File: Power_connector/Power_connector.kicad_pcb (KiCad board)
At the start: 2 copper layers, 33 parts, among them J1 XT60_F, J10 XT60_F, J11 XT60_F, J12 XT60_F, J2 XT60_Male, J3 XT60_F, J4 XT60_F, J5 Screw_Terminal_01x02, J6 XT60_F, J7 XT60_F, J8 XT60_F, J9 XT60_F, Q1 IRFS7530, Q2 IRFS7530, Q3 IRFS7530

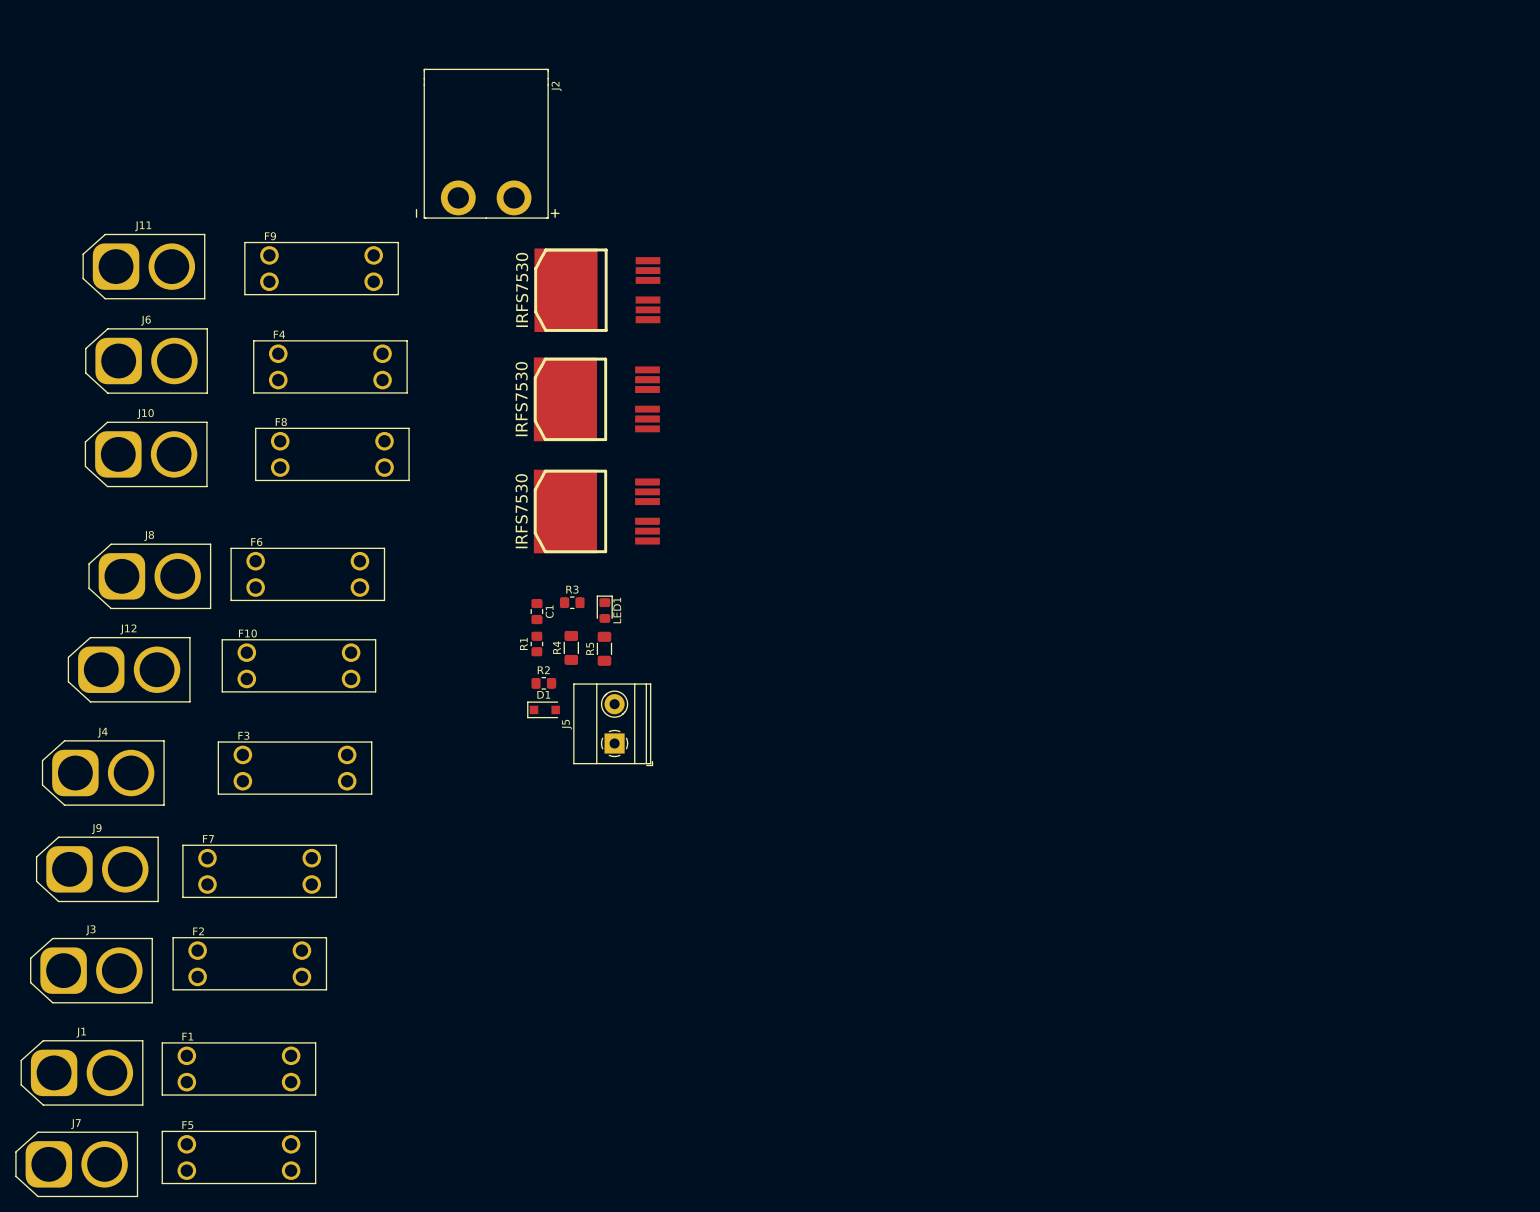
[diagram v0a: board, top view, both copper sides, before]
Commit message: added power board
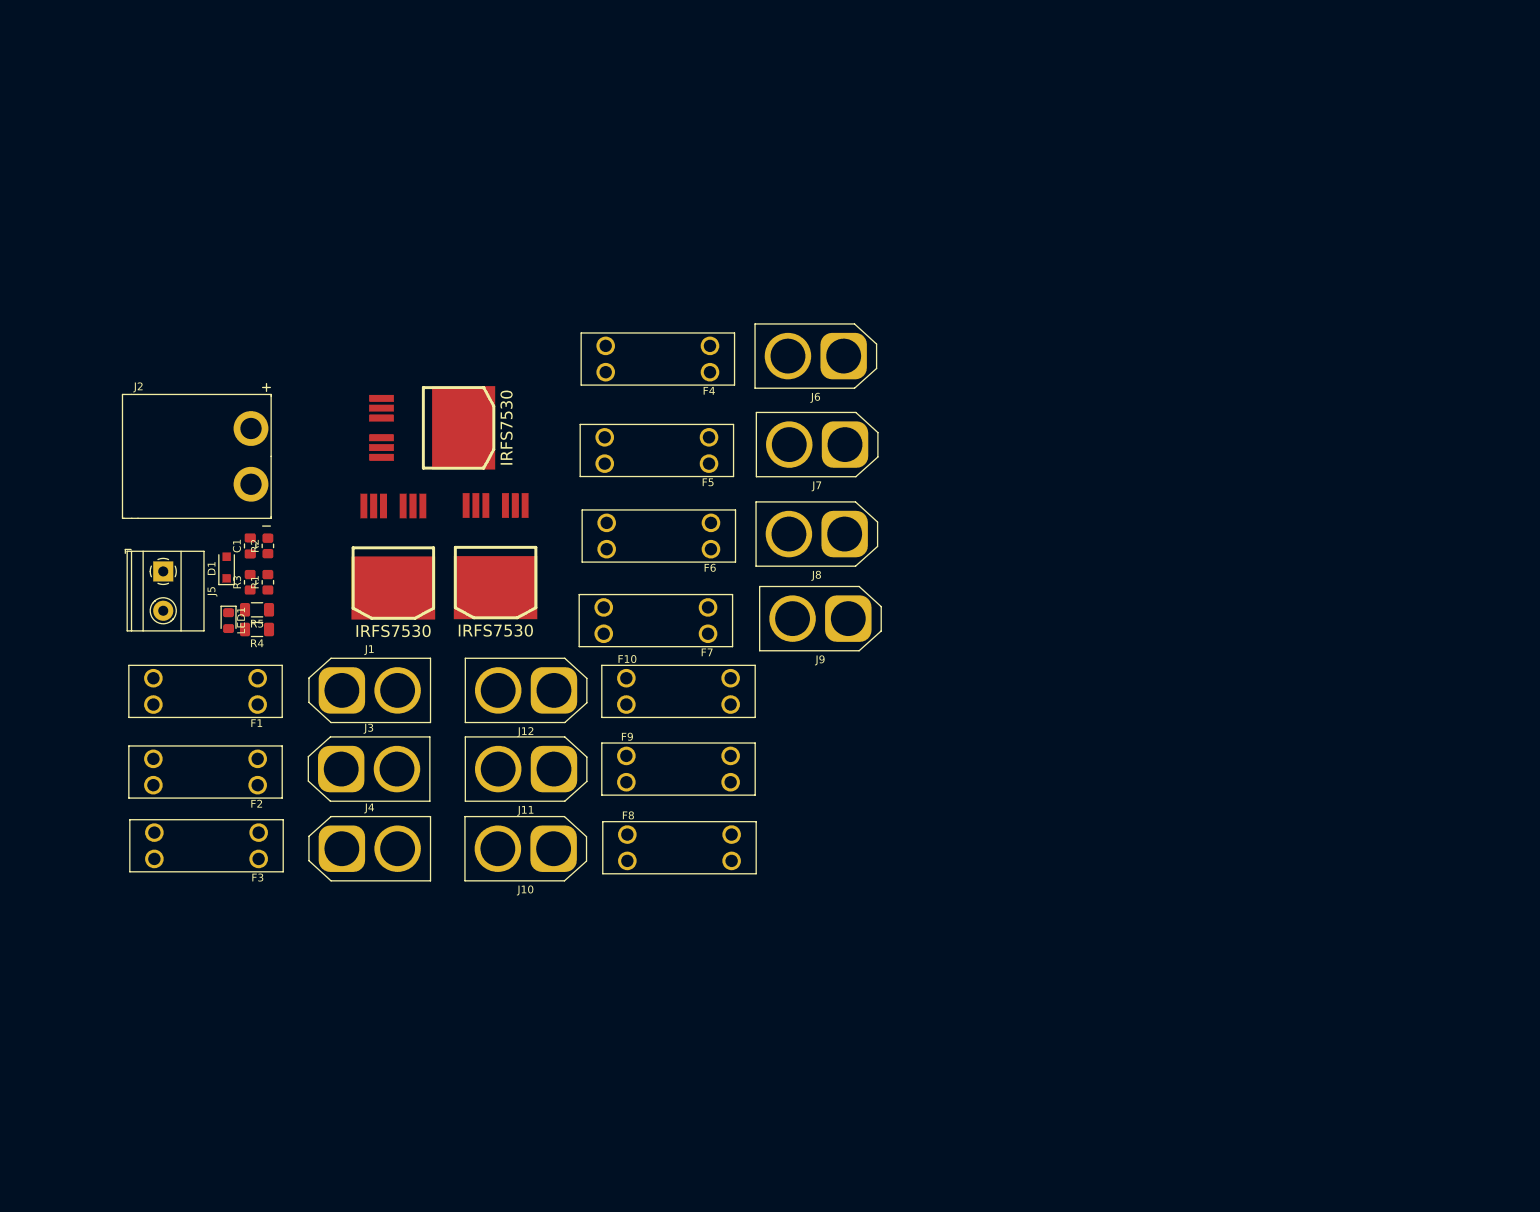
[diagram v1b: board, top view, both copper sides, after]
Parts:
- moved J7 138.6 mm to (162.5, 96.0), turned to 180 degrees
- moved F5 106.1 mm to (138.2, 96.8), turned to 180 degrees
- moved J9 105.7 mm to (162.9, 118.5), turned to 180 degrees
- moved J6 93.6 mm to (162.3, 84.6), turned to 180 degrees
- moved J8 93.5 mm to (162.4, 107.6), turned to 180 degrees
- moved J11 86.1 mm to (124.9, 137.9), turned to 180 degrees
- moved F9 79.4 mm to (141.0, 137.9)
- moved J10 75.9 mm to (124.8, 148.2), turned to 180 degrees
- moved F8 67.8 mm to (141.1, 148.1)
- moved J5 62.4 mm to (74.4, 112.4), turned to -90 degrees
- moved J1 61.8 mm to (97.5, 127.8)
- moved F7 60.6 mm to (138.0, 118.7), turned to 180 degrees
- moved J12 58.5 mm to (124.9, 127.8), turned to 180 degrees
- moved J2 53.6 mm to (79.8, 97.5), turned to 180 degrees
- moved F10 49.1 mm to (141.0, 127.9)
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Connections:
- J2 pad 1: +24V -> -BATT
- J2 pad 2: -BATT -> +24V

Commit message: power board
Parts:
- added D10: 1N4001, Diode_THT:D_DO-41_SOD81_P10.16mm_Horizontal, F.Cu at (171.4, 94.0)
- added D11: 1N4001, Diode_THT:D_DO-41_SOD81_P10.16mm_Horizontal, F.Cu at (195.6, 94.0)
- added D12: 1N4001, Diode_THT:D_DO-41_SOD81_P10.16mm_Horizontal, F.Cu at (219.7, 94.0)
- added D13: 1N4001, Diode_THT:D_DO-41_SOD81_P10.16mm_Horizontal, F.Cu at (243.8, 94.0)
- added D2: 1N4001, Diode_THT:D_DO-41_SOD81_P10.16mm_Horizontal, F.Cu at (121.9, 63.2)
- added D3: 1N4001, Diode_THT:D_DO-41_SOD81_P10.16mm_Horizontal, F.Cu at (147.3, 63.3)
- added D4: 1N4001, Diode_THT:D_DO-41_SOD81_P10.16mm_Horizontal, F.Cu at (171.4, 63.3)
- added D5: 1N4001, Diode_THT:D_DO-41_SOD81_P10.16mm_Horizontal, F.Cu at (194.3, 63.3)
- added D6: 1N4001, Diode_THT:D_DO-41_SOD81_P10.16mm_Horizontal, F.Cu at (219.7, 63.3)
- added D7: 1N4001, Diode_THT:D_DO-41_SOD81_P10.16mm_Horizontal, F.Cu at (243.8, 63.3)
- added D8: 1N4001, Diode_THT:D_DO-41_SOD81_P10.16mm_Horizontal, F.Cu at (123.2, 94.0)
- added D9: 1N4001, Diode_THT:D_DO-41_SOD81_P10.16mm_Horizontal, F.Cu at (147.3, 94.0)
- added F11: 3557-2, PolyuRobotics:FUSE_3557-2, F.Cu at (213.4, 87.6)
- added F12: 3557-2, PolyuRobotics:FUSE_3557-2, F.Cu at (237.5, 87.6)
- added J13: XT60_F, Connector_AMASS:AMASS_XT60-F_1x02_P7.20mm_Vertical, F.Cu at (207.0, 96.7)
- added J14: XT60_F, Connector_AMASS:AMASS_XT60-F_1x02_P7.20mm_Vertical, F.Cu at (231.1, 96.7)
- added Q4: IRFS7530, sparkparts:D2PAK-7-GDS, F.Cu at (96.5, 62.2)
- moved F3 114.6 mm to (165.1, 71.1), turned to 0 degrees
- moved J4 106.1 mm to (159.0, 61.8), turned to 90 degrees
- moved F6 105.6 mm to (237.5, 71.1), turned to 0 degrees
- moved F2 90.8 mm to (141.0, 71.1), turned to 0 degrees
- moved J3 84.8 mm to (134.6, 61.8), turned to 90 degrees
- moved J8 82.6 mm to (231.1, 61.8), turned to 90 degrees
- moved F5 79.4 mm to (213.4, 71.1), turned to 0 degrees
- moved F1 67.7 mm to (116.8, 71.1), turned to 0 degrees
- moved J1 67.2 mm to (110.5, 61.8), turned to 90 degrees
- moved J12 65.8 mm to (182.9, 96.7), turned to -90 degrees
- moved F10 62.8 mm to (189.2, 87.6)
- moved F8 60.5 mm to (141.0, 87.6)
- moved J7 56.2 mm to (207.0, 61.8), turned to 90 degrees
- moved F9 55.8 mm to (165.1, 87.6)
- moved J9 55.5 mm to (111.8, 96.9), turned to -90 degrees
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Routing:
- net +24V: track 0.00 -> 414.4 mm
- net GND: track 0.00 -> 378.7 mm
- net /SW_NC: track 0.00 -> 132.4 mm
- net Net-(F7-Pad1): track 0.00 -> 11.5 mm
- net Net-(F3-Pad1): track 0.00 -> 11.3 mm
- net Net-(F2-Pad1): track 0.00 -> 11.2 mm
- net Net-(F6-Pad1): track 0.00 -> 11.2 mm
- net Net-(F5-Pad1): track 0.00 -> 11.2 mm
- net Net-(F4-Pad1): track 0.00 -> 11.2 mm
- net Net-(F1-Pad1): track 0.00 -> 11.2 mm
- net Net-(F8-Pad1): track 0.00 -> 11.0 mm
- net Net-(F12-Pad1): track 0.00 -> 11.0 mm
- net Net-(F11-Pad1): track 0.00 -> 11.0 mm
- net Net-(F10-Pad1): track 0.00 -> 11.0 mm
- net Net-(F9-Pad1): track 0.00 -> 10.7 mm
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- added copper zone on B.Cu, net -BATT
- added copper zone on F.Cu, net -BATT
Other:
- board outline added: 184.8 x 60.3 mm

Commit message: power board
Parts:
- moved D7 4.70 mm to (239.5, 65.2)
- moved D13 4.22 mm to (239.6, 93.5)
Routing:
- net GND: track 378.7 -> 562.0 mm, vias 0 -> 42
- net +24V: track 414.4 -> 543.9 mm
- net Net-(F12-Pad1): track 11.0 -> 0.54 mm
- net -BATT: vias 0 -> 165
- net (no net): vias 0 -> 2
- added copper zone on B.Cu, net GND
- added copper zone on F.Cu, net GND

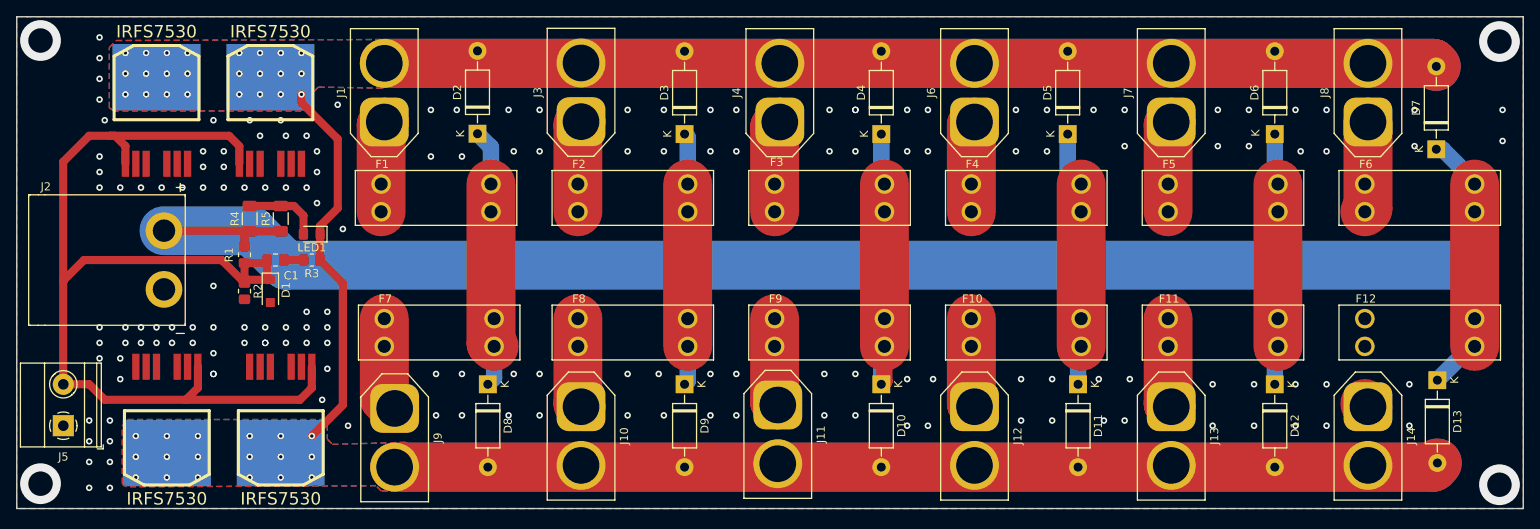
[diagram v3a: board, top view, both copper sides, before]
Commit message: power connector added
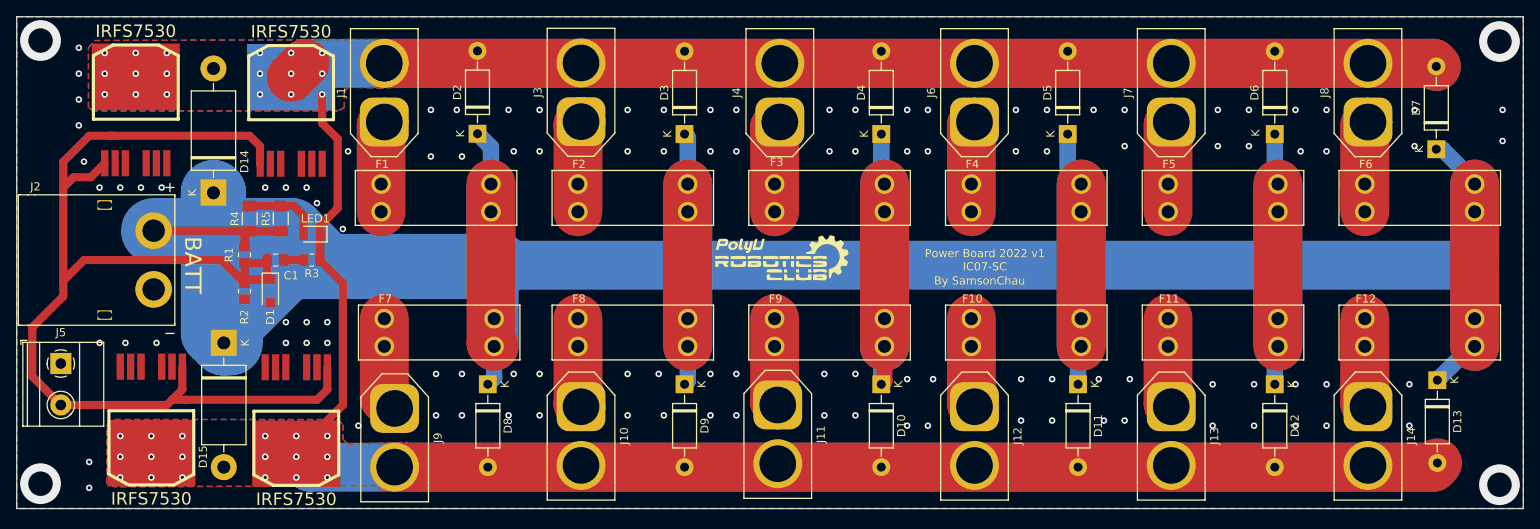
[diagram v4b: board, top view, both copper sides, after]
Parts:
- added D14: 1N5408, Diode_THT:D_DO-201AD_P15.24mm_Horizontal, F.Cu at (89.5, 70.5)
- added D15: 1N5408, Diode_THT:D_DO-201AD_P15.24mm_Horizontal, F.Cu at (90.8, 88.9)
- added G***: LOGO, PolyuRobotics:Club_logo, F.Cu at (159.4, 78.7)
- added G***: LOGO, PolyuRobotics:Club_logo, B.Cu at (80.6, 62.9)
- R1: value 1M -> 1.5M
- R2: value 1M -> 400k
- moved J5 7.63 mm to (70.8, 91.4), turned to -90 degrees
- moved Q1 2.54 mm to (80.0, 62.2)
- moved Q4 2.54 mm to (99.1, 62.2)
- moved Q3 1.91 mm to (99.7, 96.6)
- moved Q2 1.90 mm to (81.9, 96.5)
- moved J2 1.27 mm to (76.2, 78.7)
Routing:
- net +24V: track 543.9 -> 621.5 mm
- net GND: track 562.0 -> 585.0 mm, vias 42 -> 36
- net /SW_NC: track 132.4 -> 144.5 mm
- net Net-(F12-Pad1): track 0.54 -> 11.0 mm
- net -BATT: vias 165 -> 112
- net (no net): vias 2 -> 4
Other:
- board text added: "BATT"
- board text added: "By SamsonChau"
- board text added: "Power Board 2022 v1 IC07-SC"

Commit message: powerboard mod
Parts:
- removed G*** (x2): LOGO, PolyuRobotics:Club_logo
- removed Q3, Q4: IRFS7530, sparkparts:D2PAK-7-GDS
- added LED2: power, LED_SMD:LED_0805_2012Metric_Pad1.15x1.40mm_HandSolder, F.Cu at (98.6, 125.5)
- added R10: 10M, Resistor_SMD:R_0805_2012Metric, F.Cu at (114.8, 119.7)
- added R11: 10M, Resistor_SMD:R_0805_2012Metric, F.Cu at (139.7, 119.6)
- added R12: 10M, Resistor_SMD:R_0805_2012Metric, F.Cu at (165.4, 119.7)
- added R13: 10M, Resistor_SMD:R_0805_2012Metric, F.Cu at (114.6, 70.1)
- added R14: 10M, Resistor_SMD:R_0805_2012Metric, F.Cu at (127.3, 119.8)
- added R15: 10M, Resistor_SMD:R_0805_2012Metric, F.Cu at (165.6, 70.3)
- added R16: 10M, Resistor_SMD:R_0805_2012Metric, F.Cu at (152.2, 119.8)
- added R17: 10M, Resistor_SMD:R_0805_2012Metric, F.Cu at (140.2, 70.0)
- added R18: 10M, Resistor_SMD:R_0805_2012Metric, F.Cu at (178.3, 119.6)
- added R6: 10M, Resistor_SMD:R_0805_2012Metric, F.Cu at (127.5, 69.8)
- added R7: 1.5M, Resistor_SMD:R_0805_2012Metric_Pad1.20x1.40mm_HandSolder, F.Cu at (88.9, 119.9)
- added R8: 400k, Resistor_SMD:R_0805_2012Metric_Pad1.20x1.40mm_HandSolder, F.Cu at (95.5, 120.4)
- added R9: 1K, Resistor_SMD:R_0805_2012Metric_Pad1.20x1.40mm_HandSolder, F.Cu at (86.3, 119.9)
- D1: value Zener -> 1N5408; footprint Diode_SMD:D_SOD-123F -> Diode_THT:D_DO-201AD_P15.24mm_Horizontal
- D10, D11, D12, D13, D3, D4, D5, D7, D8, D9: value 1N4001 -> indicator; footprint Diode_THT:D_DO-41_SOD81_P10.16mm_Horizontal -> LED_SMD:LED_0805_2012Metric
- D14, D15: value 1N5408 -> indicator; footprint Diode_THT:D_DO-201AD_P15.24mm_Horizontal -> LED_SMD:LED_0805_2012Metric
- D2: value 1N4001 -> 1N5408; footprint Diode_THT:D_DO-41_SOD81_P10.16mm_Horizontal -> Diode_THT:D_DO-201AD_P15.24mm_Horizontal
- D6: value 1N4001 -> Zener; footprint Diode_THT:D_DO-41_SOD81_P10.16mm_Horizontal -> Diode_SMD:D_SOD-123F
- J4: value XT60_F -> E_Stop; footprint Connector_AMASS:AMASS_XT60-F_1x02_P7.20mm_Vertical -> TerminalBlock_Phoenix:TerminalBlock_Phoenix_MKDS-1,5-2-5.08_1x02_P5.08mm_Horizontal
- J5: value Screw_Terminal_01x02 -> XT60_F; footprint TerminalBlock_Phoenix:TerminalBlock_Phoenix_MKDS-1,5-2-5.08_1x02_P5.08mm_Horizontal -> Connector_AMASS:AMASS_XT60-F_1x02_P7.20mm_Vertical
- LED1: value power -> BATT
- Q1, Q2: moved to B.Cu
- R1: value 1.5M -> 10M; footprint Resistor_SMD:R_0805_2012Metric_Pad1.20x1.40mm_HandSolder -> Resistor_SMD:R_0805_2012Metric
- R2: value 400k -> 10M; footprint Resistor_SMD:R_0805_2012Metric_Pad1.20x1.40mm_HandSolder -> Resistor_SMD:R_0805_2012Metric
- R3: value 1K -> 16.5K; footprint Resistor_SMD:R_0805_2012Metric_Pad1.20x1.40mm_HandSolder -> Resistor_SMD:R_1206_3216Metric_Pad1.30x1.75mm_HandSolder
- R4: value 16.5K -> 10M; footprint Resistor_SMD:R_1206_3216Metric_Pad1.30x1.75mm_HandSolder -> Resistor_SMD:R_0805_2012Metric
- moved D6 139.2 mm to (93.0, 120.9)
- moved D7 137.8 mm to (114.8, 123.8)
- moved J6 101.0 mm to (108.3, 130.0)
- moved J7 100.1 mm to (133.7, 130.0)
- moved J8 99.2 mm to (159.1, 130.0)
- moved D15 94.2 mm to (178.3, 123.8), turned to 90 degrees
- moved D13 92.6 mm to (152.1, 123.7), turned to 90 degrees
- moved F4 88.3 mm to (108.2, 106.1), turned to 90 degrees
- moved F5 87.1 mm to (133.6, 106.1), turned to 90 degrees
- moved R2 85.9 mm to (178.3, 70.0), turned to 90 degrees
- moved F6 85.8 mm to (159.1, 106.1), turned to 90 degrees
- moved D1 83.8 mm to (179.8, 91.9), turned to 90 degrees
- moved J13 81.9 mm to (133.9, 59.9)
- moved F11 79.8 mm to (133.6, 83.8), turned to -90 degrees
- moved D11 74.5 mm to (127.3, 123.7), turned to 90 degrees
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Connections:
- D1 pad 1: /SW_NC -> +24V
- D1 pad 2: -BATT -> GND
- D10 pad 1: +24V -> GND
- D10 pad 2: GND -> Net-(D10-Pad2)
- D11 pad 1: +24V -> GND
- D11 pad 2: GND -> Net-(D11-Pad2)
- D12 pad 1: +24V -> unconnected-(D12-Pad1)
- D12 pad 2: GND -> Net-(D12-Pad2)
- D13 pad 1: +24V -> GND
- D13 pad 2: GND -> Net-(D13-Pad2)
- D14 pad 1: +24V -> GND
- D14 pad 2: GND -> Net-(D14-Pad2)
- D15 pad 1: +24V -> GND
- D15 pad 2: GND -> Net-(D15-Pad2)
- D3 pad 1: +24V -> GND
- D3 pad 2: GND -> Net-(D3-Pad2)
- D4 pad 1: +24V -> GND
- D4 pad 2: GND -> Net-(D4-Pad2)
- D5 pad 1: +24V -> unconnected-(D5-Pad1)
- D5 pad 2: GND -> Net-(D5-Pad2)
- D6 pad 1: +24V -> /SW_NC
- D6 pad 2: GND -> +24V
- D7 pad 1: +24V -> GND
- D7 pad 2: GND -> Net-(D7-Pad2)
- D8 pad 1: +24V -> GND
- D8 pad 2: GND -> Net-(D8-Pad2)
- D9 pad 1: +24V -> GND
- D9 pad 2: GND -> Net-(D9-Pad2)
- J1 pad 1: Net-(F1-Pad1) -> GND
- J1 pad 2: GND -> Net-(F1-Pad1)
- J10 pad 1: Net-(F8-Pad1) -> GND
- J10 pad 2: GND -> Net-(F8-Pad1)
- J11 pad 1: Net-(F9-Pad1) -> GND
- J11 pad 2: GND -> Net-(F9-Pad1)
- J12 pad 1: Net-(F10-Pad1) -> GND
- J12 pad 2: GND -> Net-(F10-Pad1)
- J13 pad 1: Net-(F11-Pad1) -> GND
- J13 pad 2: GND -> Net-(F11-Pad1)
- J14 pad 1: Net-(F12-Pad1) -> GND
- J14 pad 2: GND -> Net-(F12-Pad1)
- J2 pad 1: -BATT -> GND
- J2 pad 2: +24V -> +BATT
- J3 pad 1: Net-(F2-Pad1) -> GND
- J3 pad 2: GND -> Net-(F2-Pad1)
- J4 pad 1: Net-(F3-Pad1) -> +24V
- J4 pad 2: GND -> /SW_NC
- J5 pad 1: -BATT -> GND
- J5 pad 2: /SW_NC -> Net-(F3-Pad1)
- J6 pad 1: Net-(F4-Pad1) -> GND
- J6 pad 2: GND -> Net-(F4-Pad1)
- J7 pad 1: Net-(F5-Pad1) -> GND
- J7 pad 2: GND -> Net-(F5-Pad1)
- J8 pad 1: Net-(F6-Pad1) -> GND
- J8 pad 2: GND -> Net-(F6-Pad1)
- J9 pad 1: Net-(F7-Pad1) -> GND
- J9 pad 2: GND -> Net-(F7-Pad1)
- Q1 pad D: GND -> +BATT
- Q1 pad S: -BATT -> +24V
- Q2 pad D: GND -> +BATT
- Q2 pad S: -BATT -> +24V
- R1 pad 1: +24V -> +BATT
- R1 pad 2: /SW_NC -> Net-(LED1-Pad2)
- R2 pad 1: /SW_NC -> Net-(F1-Pad1)
- R2 pad 2: -BATT -> Net-(D3-Pad2)
- R3 pad 1: GND -> +24V
- R3 pad 2: Net-(C1-Pad1) -> Net-(LED2-Pad2)
- R4 pad 1: +24V -> Net-(F2-Pad1)
- R4 pad 2: Net-(LED1-Pad2) -> Net-(D4-Pad2)
- R5 pad 2: Net-(LED1-Pad2) -> Net-(LED2-Pad2)
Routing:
- net +24V: track 621.5 -> 27.1 mm
- net GND: track 585.0 -> 0.00 mm, vias 36 -> 13
- net /SW_NC: track 144.5 -> 87.1 mm, vias 0 -> 1
- net +BATT: track 0.00 -> 36.4 mm
- net Net-(F2-Pad1): track 11.2 -> 31.8 mm
- net Net-(F3-Pad1): track 11.3 -> 31.3 mm
- net Net-(F7-Pad1): track 11.5 -> 31.1 mm
- net Net-(F6-Pad1): track 11.2 -> 21.9 mm
- net Net-(F9-Pad1): track 10.7 -> 21.0 mm
- net Net-(F8-Pad1): track 11.0 -> 20.9 mm
- net Net-(F1-Pad1): track 11.2 -> 21.0 mm
- net Net-(F12-Pad1): track 11.0 -> 20.8 mm
- net Net-(F11-Pad1): track 11.0 -> 20.5 mm
- net Net-(F10-Pad1): track 11.0 -> 20.4 mm
- net Net-(F4-Pad1): track 11.2 -> 20.5 mm
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- added copper zone on B.Cu, net +24V
- added copper zone on F.Cu, net +24V
- added copper zone on B.Cu, net +BATT
- removed copper zone on B.Cu, net -BATT
- removed copper zone on F.Cu, net -BATT
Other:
- board size 184.8 x 60.3 mm -> 107.2 x 80.8 mm
- board text removed: "BATT"
- board text removed: "By SamsonChau"
- board text removed: "Power Board 2022 v1 IC07-SC"

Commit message: ESP,Power board update
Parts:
- added G***: LOGO, PolyuRobotics:Club_logo, F.Cu at (93.7, 110.7)
- moved C1 1.27 mm to (87.4, 124.7)
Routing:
- net +24V: track 27.1 -> 50.1 mm
- net Net-(C1-Pad1): track 2.56 -> 3.83 mm
- net /SW_NC: track 87.1 -> 88.4 mm
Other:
- board text added: "17K"
- board text added: "Created for:"
- board text added: "Power Board Rev 1.5 By Samson Chau High-Side Switch version 2022-06-23"
